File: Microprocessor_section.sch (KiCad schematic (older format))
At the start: 14 parts

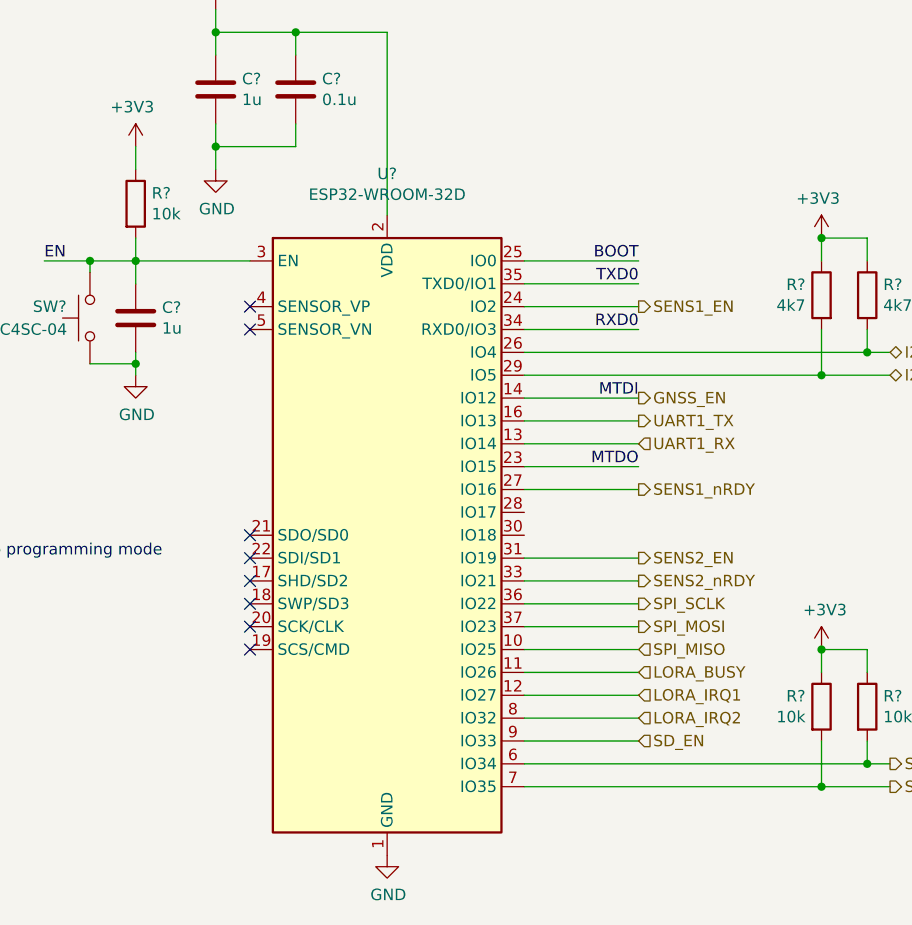
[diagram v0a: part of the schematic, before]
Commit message: Change mcp reset pin cap to 100n, add uart2 lines
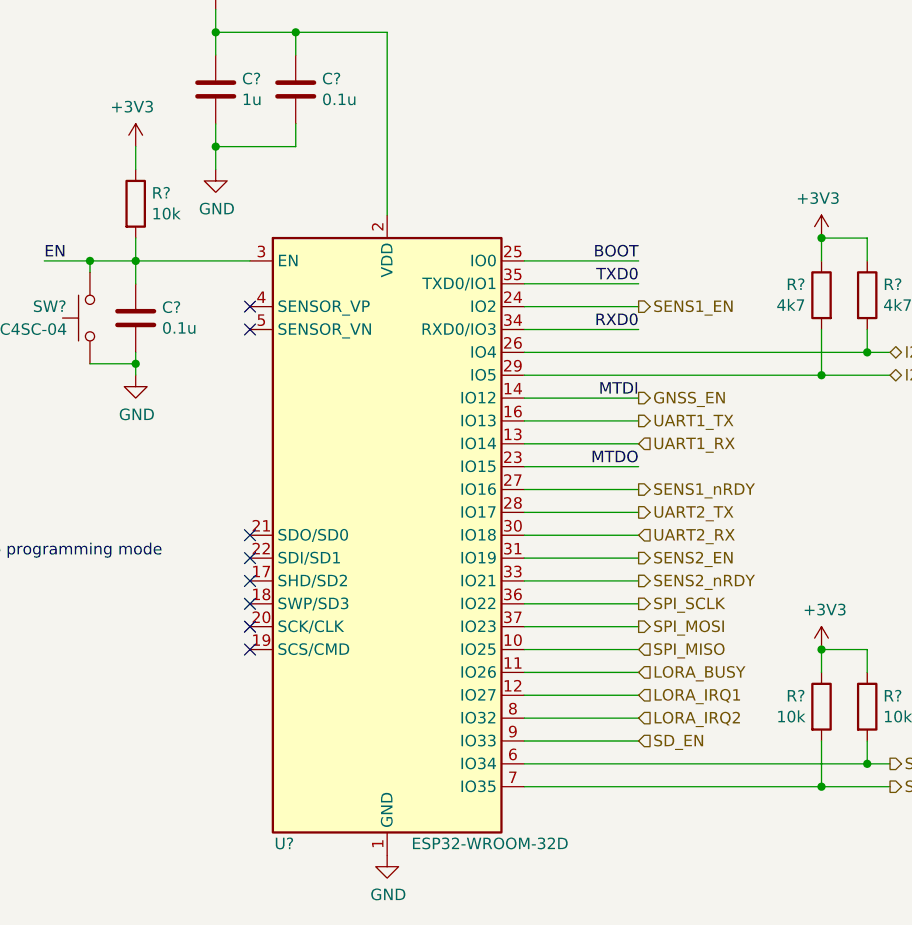
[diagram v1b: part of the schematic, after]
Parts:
- C?: value 1u -> 0.1u
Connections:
- net UART2_TX: now reaches U?.28 (IO17)
- net UART2_RX: now reaches U?.30 (IO18)
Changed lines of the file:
@@
 P 5400 3050
 F 0 "C?" H 5515 3096 50  0000 L CNN
-F 1 "1u" H 5515 3005 50  0000 L CNN
+F 1 "0.1u" H 5515 3005 50  0000 L CNN
 F 2 "" H 5438 2900 50  0001 C CNN
 F 3 "~" H 5400 3050 50  0001 C CNN
@@
 U 1 1 60AF9B80
 P 6500 4000
-F 0 "U?" H 6500 5581 50  0000 C CNN
-F 1 "ESP32-WROOM-32D" H 6500 5490 50  0000 C CNN
+F 0 "U?" H 6050 2650 50  0000 C CNN
+F 1 "ESP32-WROOM-32D" H 6950 2650 50  0000 C CNN
 F 2 "RF_Module:ESP32-WROOM-32" H 6500 2500 50  0001 C CNN
 F 3 "https://www.espressif.com/sites/default/files/documentation/esp32-wroom-32d_esp32-wroom-32u_datasheet_en.pdf" H 6200 4050 50  0001 C CNN
@@
 Wire Wire Line
 	4100 4100 4100 4600
+Text HLabel 7600 3900 2    50   Output ~ 0
+UART2_TX
+Text HLabel 7600 4000 2    50   Input ~ 0
+UART2_RX
+Wire Wire Line
+	7600 4000 7100 4000
+Wire Wire Line
+	7100 3900 7600 3900
 $EndSCHEMATC

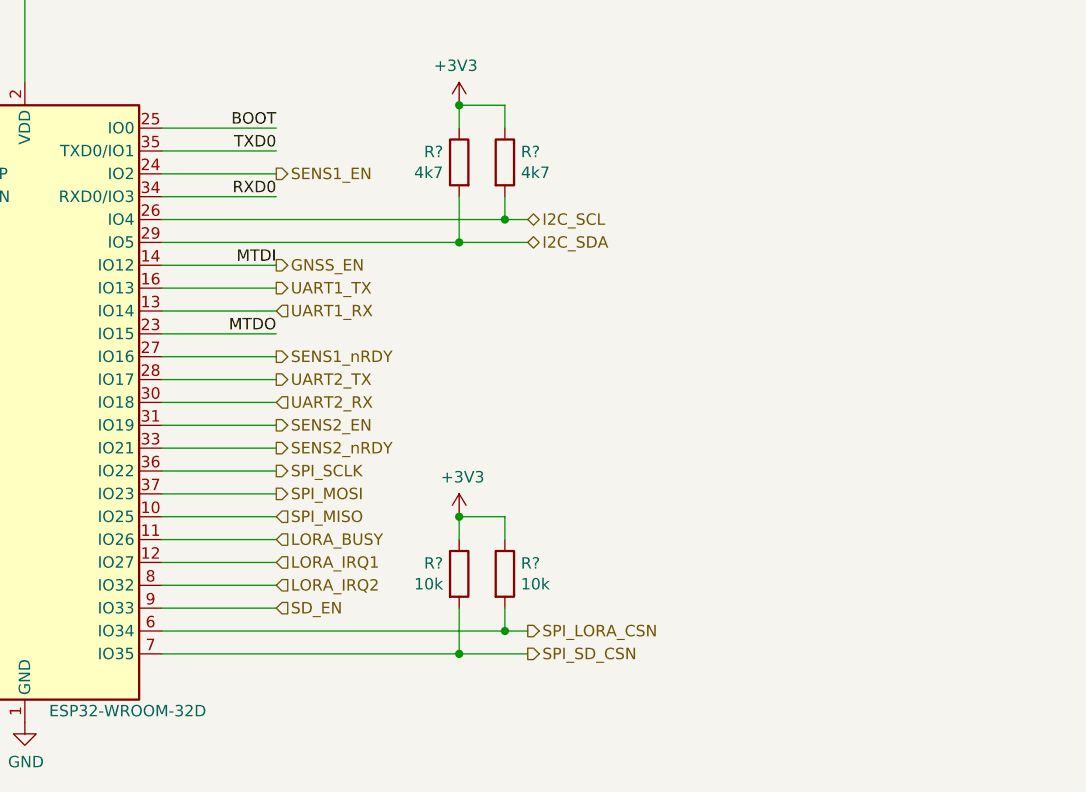
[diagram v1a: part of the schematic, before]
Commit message: Rearranged IO connections to take advantage of hardware interfaces where possible
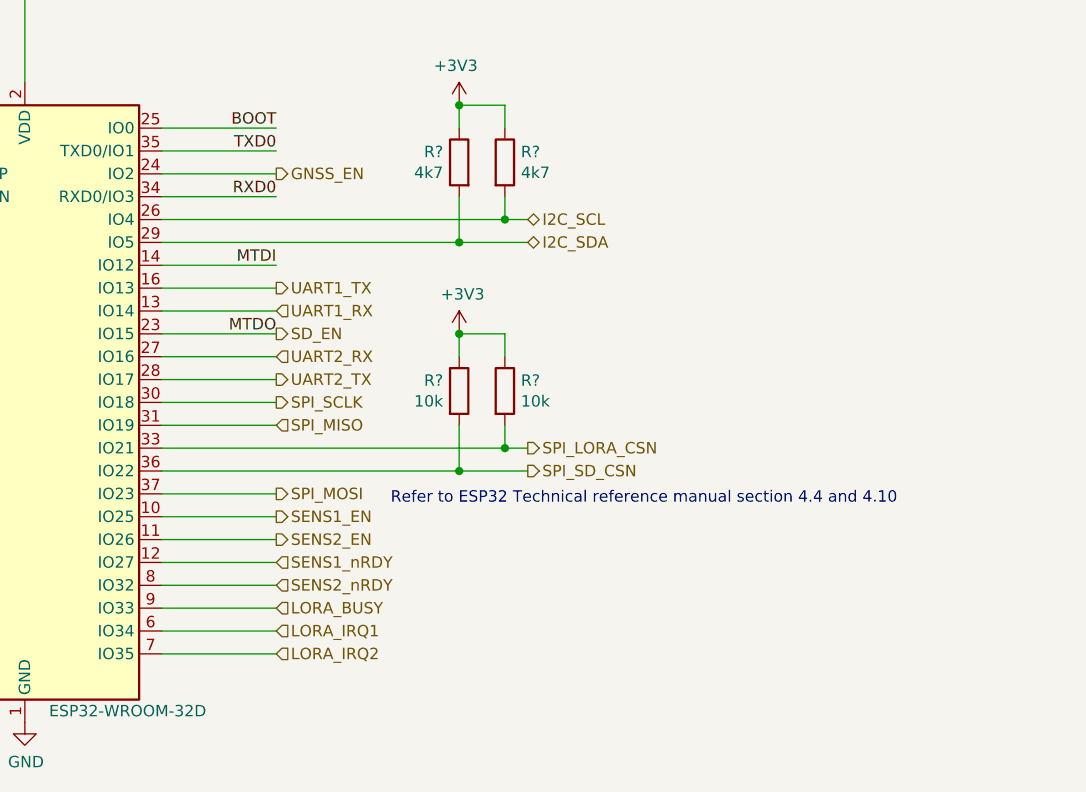
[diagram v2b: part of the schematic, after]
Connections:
- net MTDO is gone; now on net SD_EN: JP?.2 (Pin_2), U?.23 (IO15)
- net GNSS_EN: now also U?.24 (IO2); no longer U?.14 (IO12)
- net LORA_BUSY: now also U?.9 (IO33); no longer U?.11 (IO26)
- net LORA_IRQ1: now also U?.6 (IO34); no longer U?.12 (IO27)
- net LORA_IRQ2: now also U?.7 (IO35); no longer U?.8 (IO32)
- net SD_EN: no longer U?.9 (IO33)
- net SENS1_EN: now also U?.10 (IO25); no longer U?.24 (IO2)
- net SENS1_nRDY: now also U?.12 (IO27); no longer U?.27 (IO16)
- net SENS2_EN: now also U?.11 (IO26); no longer U?.31 (IO19)
- net SENS2_nRDY: now also U?.8 (IO32); no longer U?.33 (IO21)
- net SPI_LORA_CSN: now also U?.33 (IO21); no longer U?.6 (IO34)
- net SPI_MISO: now also U?.31 (IO19); no longer U?.10 (IO25)
- net SPI_SCLK: now also U?.30 (IO18); no longer U?.36 (IO22)
- net SPI_SD_CSN: now also U?.36 (IO22); no longer U?.7 (IO35)
- net UART2_RX: now also U?.27 (IO16); no longer U?.30 (IO18)
- new net MTDI: U?.14 (IO12)
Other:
- note added: "Refer to ESP32 Technical reference manual section 4.4 and 4.10\n"
- moved on the sheet: R?
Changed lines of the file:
@@
 Connection ~ 8400 2700
 Wire Wire Line
-	8600 5000 8700 5000
-Connection ~ 8600 5000
-Wire Wire Line
-	8600 4900 8600 5000
-Wire Wire Line
-	8400 5100 8700 5100
-Connection ~ 8400 5100
-Wire Wire Line
-	8400 4900 8400 5100
-Wire Wire Line
-	7100 5000 8600 5000
-Wire Wire Line
-	7100 5100 8400 5100
+	8600 4200 8700 4200
+Connection ~ 8600 4200
+Wire Wire Line
+	8600 4100 8600 4200
+Wire Wire Line
+	8400 4300 8700 4300
+Connection ~ 8400 4300
+Wire Wire Line
+	8400 4100 8400 4300
+Wire Wire Line
+	7100 4200 8600 4200
+Wire Wire Line
+	7100 4300 8400 4300
 Wire Wire Line
 	8600 3200 8700 3200
@@
 	8400 2700 8600 2700
 Wire Wire Line
-	8400 4500 8600 4500
-Wire Wire Line
-	8600 4500 8600 4600
+	8400 3700 8600 3700
+Wire Wire Line
+	8600 3700 8600 3800
 $Comp
 L power:GND #PWR?
@@
 $EndComp
 Wire Wire Line
+	7100 5100 7600 5100
+Wire Wire Line
+	7100 5000 7600 5000
+Wire Wire Line
 	7100 4900 7600 4900
 Wire Wire Line
+	7100 4100 7600 4100
+Wire Wire Line
+	7100 4400 7600 4400
+Wire Wire Line
+	7100 4000 7600 4000
+Wire Wire Line
 	7100 4800 7600 4800
 Wire Wire Line
+	7100 4600 7600 4600
+Wire Wire Line
 	7100 4700 7600 4700
 Wire Wire Line
-	7100 4600 7600 4600
-Wire Wire Line
-	7100 4500 7600 4500
-Wire Wire Line
-	7100 4400 7600 4400
-Wire Wire Line
-	7100 4300 7600 4300
-Wire Wire Line
-	7100 4200 7600 4200
-Wire Wire Line
-	7100 4100 7600 4100
-Wire Wire Line
-	7100 3800 7600 3800
-Wire Wire Line
 	7100 3000 7600 3000
 Wire Wire Line
 	7100 3400 7600 3400
-Text HLabel 7600 4500 2    50   Input ~ 0
+Text HLabel 7600 4100 2    50   Input ~ 0
 SPI_MISO
 Text HLabel 7600 4400 2    50   Output ~ 0
 SPI_MOSI
-Text HLabel 7600 4300 2    50   Output ~ 0
+Text HLabel 7600 4000 2    50   Output ~ 0
 SPI_SCLK
+Text HLabel 7600 3700 2    50   Output ~ 0
+SD_EN
+Text HLabel 7600 5100 2    50   Input ~ 0
+LORA_IRQ2
+Text HLabel 7600 5000 2    50   Input ~ 0
+LORA_IRQ1
 Text HLabel 7600 4900 2    50   Input ~ 0
-SD_EN
+LORA_BUSY
+Text HLabel 7600 3000 2    50   Output ~ 0
+GNSS_EN
 Text HLabel 7600 4800 2    50   Input ~ 0
-LORA_IRQ2
+SENS2_nRDY
+Text HLabel 7600 4600 2    50   Output ~ 0
+SENS2_EN
 Text HLabel 7600 4700 2    50   Input ~ 0
-LORA_IRQ1
-Text HLabel 7600 4600 2    50   Input ~ 0
-LORA_BUSY
-Text HLabel 7600 3400 2    50   Output ~ 0
-GNSS_EN
-Text HLabel 7600 4200 2    50   Output ~ 0
-SENS2_nRDY
-Text HLabel 7600 4100 2    50   Output ~ 0
-SENS2_EN
-Text HLabel 7600 3800 2    50   Output ~ 0
 SENS1_nRDY
-Text HLabel 7600 3000 2    50   Output ~ 0
+Text HLabel 7600 4500 2    50   Output ~ 0
 SENS1_EN
 Wire Wire Line
@@
 	6100 1800 5750 1800
 Connection ~ 6100 1800
-Connection ~ 8400 4500
-Wire Wire Line
-	8400 4600 8400 4500
+Connection ~ 8400 3700
+Wire Wire Line
+	8400 3800 8400 3700
 $Comp
 L power:+3V3 #PWR?
 U 1 1 60A5A46E
-P 8400 4500
-F 0 "#PWR?" H 8400 4350 50  0001 C CNN
-F 1 "+3V3" H 8415 4673 50  0000 C CNN
-F 2 "" H 8400 4500 50  0001 C CNN
-F 3 "" H 8400 4500 50  0001 C CNN
-	1    8400 4500
+P 8400 3700
+F 0 "#PWR?" H 8400 3550 50  0001 C CNN
+F 1 "+3V3" H 8415 3873 50  0000 C CNN
+F 2 "" H 8400 3700 50  0001 C CNN
+F 3 "" H 8400 3700 50  0001 C CNN
+	1    8400 3700
 	1    0    0    -1
 $EndComp
@@
 L Device:R R?
 U 1 1 60A5A468
-P 8600 4750
-F 0 "R?" H 8670 4796 50  0000 L CNN
-F 1 "10k" H 8670 4705 50  0000 L CNN
-F 2 "" V 8530 4750 50  0001 C CNN
-F 3 "~" H 8600 4750 50  0001 C CNN
-	1    8600 4750
+P 8600 3950
+F 0 "R?" H 8670 3996 50  0000 L CNN
+F 1 "10k" H 8670 3905 50  0000 L CNN
+F 2 "" V 8530 3950 50  0001 C CNN
+F 3 "~" H 8600 3950 50  0001 C CNN
+	1    8600 3950
 	1    0    0    -1
 $EndComp
@@
 L Device:R R?
 U 1 1 60A5A462
-P 8400 4750
-F 0 "R?" H 8330 4796 50  0000 R CNN
-F 1 "10k" H 8330 4705 50  0000 R CNN
-F 2 "" V 8330 4750 50  0001 C CNN
-F 3 "~" H 8400 4750 50  0001 C CNN
-	1    8400 4750
+P 8400 3950
+F 0 "R?" H 8330 3996 50  0000 R CNN
+F 1 "10k" H 8330 3905 50  0000 R CNN
+F 2 "" V 8330 3950 50  0001 C CNN
+F 3 "~" H 8400 3950 50  0001 C CNN
+	1    8400 3950
 	1    0    0    -1
 $EndComp
@@
 Wire Wire Line
 	7600 3600 7100 3600
-Text HLabel 8700 5100 2    50   Output ~ 0
+Text HLabel 8700 4300 2    50   Output ~ 0
 SPI_SD_CSN
-Text HLabel 8700 5000 2    50   Output ~ 0
+Text HLabel 8700 4200 2    50   Output ~ 0
 SPI_LORA_CSN
 Text HLabel 8700 3300 2    50   BiDi ~ 0
@@
 Wire Wire Line
 	4100 4100 4100 4600
+Wire Wire Line
+	7100 3900 7600 3900
+Wire Wire Line
+	7600 3800 7100 3800
+Text HLabel 7600 3800 2    50   Input ~ 0
+UART2_RX
 Text HLabel 7600 3900 2    50   Output ~ 0
 UART2_TX
-Text HLabel 7600 4000 2    50   Input ~ 0
-UART2_RX
-Wire Wire Line
-	7600 4000 7100 4000
-Wire Wire Line
-	7100 3900 7600 3900
+Wire Wire Line
+	7600 4500 7100 4500
+Text Notes 8100 4450 0    50   ~ 0
+Refer to ESP32 Technical reference manual section 4.4 and 4.10\n
 $EndSCHEMATC
